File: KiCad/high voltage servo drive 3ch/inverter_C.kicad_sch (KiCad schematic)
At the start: 50 parts, among them U18 IPM

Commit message: prepare rev0.1 for manufacturing
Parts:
- C164, C165, C166, C167, C168, C169, C186: Generic Allowed? (none) -> yes; LCSC# (none) -> C106205; Manufacturer (none) -> YAGEO; Part number (none) -> CC0402KRX7R9BB102; cost (none) -> 0.001
- C170, C172, C175, C185: Generic Allowed? (none) -> yes; LCSC# C7393943 -> C50254; Manufacturer (none) -> Samsung Electro-Mechanics; Part number (none) -> CL31B225KBHNNNE; cost (none) -> 0.03
- C171, C173, C174, C176, C178, C179, C180, C184: Generic Allowed? (none) -> yes; LCSC# (none) -> C105882; Manufacturer (none) -> YAGEO; Part number (none) -> CC0402KRX5R9BB104; cost (none) -> 0.003
- C177, C187: Generic Allowed? (none) -> yes; LCSC# C473196 -> C7471876; Manufacturer (none) -> KNSCHA; Part number (none) -> 189RV0014; cost (none) -> 0.05
- C181, C182: Generic Allowed? (none) -> yes; Manufacturer (none) -> HUI JU; Part number (none) -> NV1812B104K102CEMN; cost (none) -> 0.1447
- C183, C197: Generic Allowed? (none) -> yes; LCSC# (none) -> C60133; Manufacturer (none) -> YAGEO; Part number (none) -> CC0402KRX7R9BB103; cost (none) -> 0.001
- D44, D45, D46, D47: Generic Allowed? (none) -> yes; LCSC# SMA2Z22A -> C7440711; Manufacturer (none) -> XCH; Part number (none) -> SMA2Z22A; cost (none) -> 0.07
- FB10, FB9: value FerriteBead -> 0; Generic Allowed? (none) -> yes; LCSC# C963878 -> C2907406; Manufacturer (none) -> FOJAN; Part number (none) -> FRC1206P000 TS; cost (none) -> 0.0015
- NT7, NT8, NT9: now not fitted
- R114, R115, R116, R117, R118, R119, R121: value 100 -> 120; Generic Allowed? (none) -> yes; LCSC# (none) -> C114758; Manufacturer (none) -> YAGEO; Part number (none) -> RC0402FR-07120RL; cost (none) -> 0.0008
- R120, R140: Generic Allowed? (none) -> yes; LCSC# (none) -> C105873; Manufacturer (none) -> YAGEO; Part number (none) -> RC0402JR-075K1L; cost (none) -> 0.0006
- R122, R123, R124, R125, R126, R127: Generic Allowed? (none) -> yes, 1% or better; LCSC # C7419996 -> (none); LCSC# (none) -> C7419996; Manufacturer (none) -> FOJAN; Part number (none) -> FRM121WFR005TM; cost (none) -> 0.03
- U18: Manufacturer (none) -> ONSEMI; now not fitted

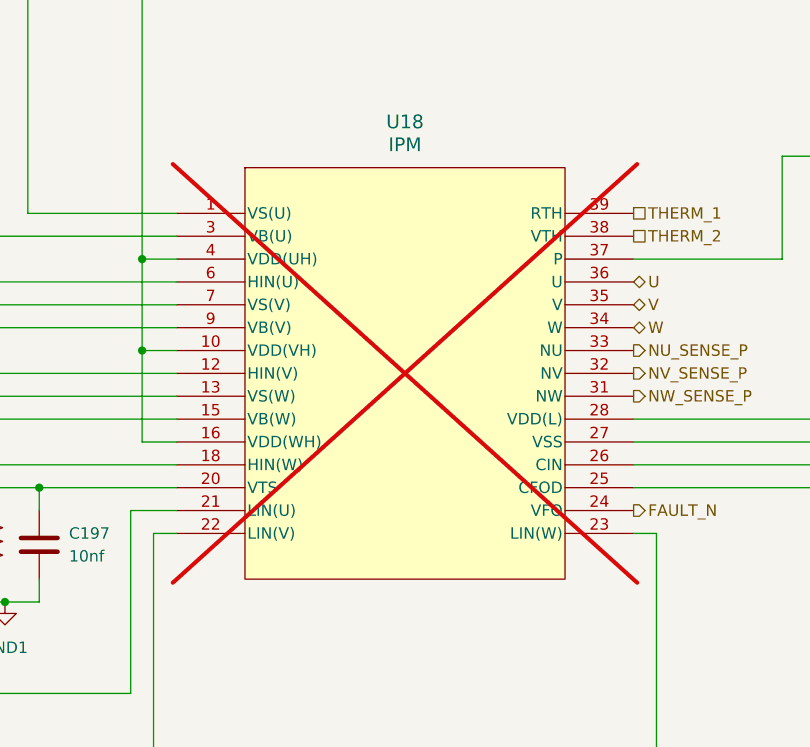
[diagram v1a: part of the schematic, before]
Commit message: update BOM and change transceivers
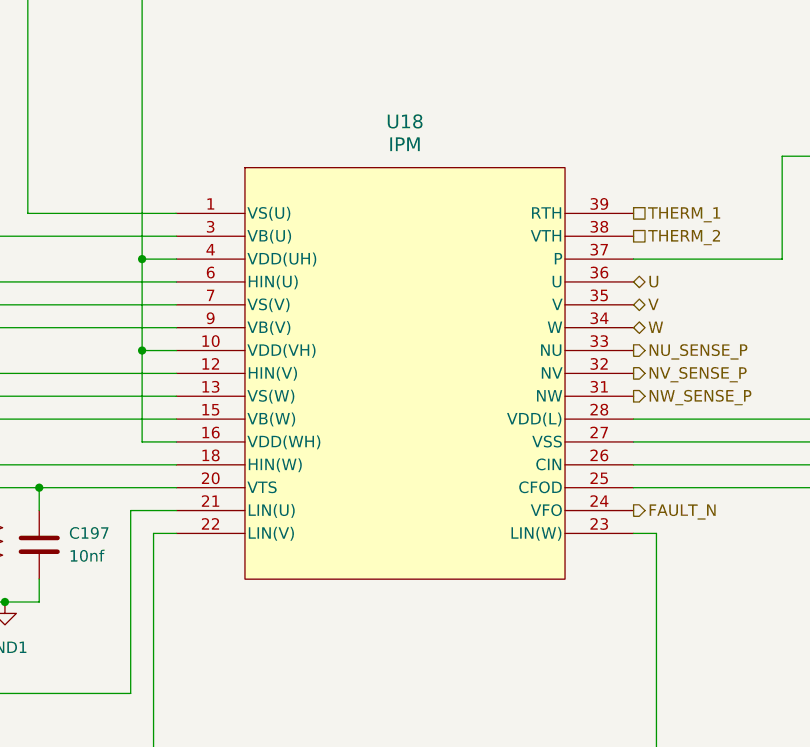
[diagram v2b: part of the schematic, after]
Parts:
- FB10, FB9: LCSC# C2907406 -> C2907288; Part number FRC1206P000 TS -> FRC0805P000 TS
- U18: footprint footprints:DIP39_54.5X31.0_MODGC_OSI -> DIP39_54.5X31.0_MODGC_OSI; now fitted
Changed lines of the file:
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@@
 		(in_bom yes)
 		(on_board yes)
-		(dnp yes)
+		(dnp no)
 		(fields_autoplaced yes)
 		(property "Reference" "U18"
@@
 			)
 		)
-		(property "Footprint" "footprints:DIP39_54.5X31.0_MODGC_OSI"
+		(property "Footprint" "DIP39_54.5X31.0_MODGC_OSI"
 			(at 184.15 121.92 0)
 			(effects
@@
 			)
 		)
-		(property "Datasheet" "IPM"
+		(property "Datasheet" "NFAM3065L4BT"
 			(at 184.15 121.92 0)
 			(effects
@@
 			)
 		)
-		(property "Description" "50v"
+		(property "Description" "Unpolarized capacitor"
 			(at 106.68 157.48 0)
 			(effects
@@
 			)
 		)
-		(property "Description" "50v"
+		(property "Description" "Unpolarized capacitor"
 			(at 116.84 203.2 0)
 			(effects
@@
 			)
 		)
-		(property "Description" "low inductance type"
+		(property "Description" "Resistor, US symbol"
 			(at 344.17 80.01 0)
 			(effects
@@
 			)
 		)
-		(property "Description" "low inductance type"
+		(property "Description" "Resistor, US symbol"
 			(at 344.17 58.42 0)
 			(effects
@@
 			)
 		)
-		(property "Description" "50v"
+		(property "Description" "Unpolarized capacitor"
 			(at 168.91 158.75 0)
 			(effects
@@
 			)
 		)
-		(property "Description" "50v"
+		(property "Description" "Unpolarized capacitor"
 			(at 328.93 158.75 0)
 			(effects
@@
 			)
 		)
-		(property "Description" "50v"
+		(property "Description" "Unpolarized capacitor"
 			(at 184.15 85.09 0)
 			(effects
@@
 			)
 		)
-		(property "Description" "63v"
+		(property "Description" "Polarized capacitor"
 			(at 335.28 143.51 0)
 			(effects
@@
 			)
 		)
-		(property "Description" "50v"
+		(property "Description" "Unpolarized capacitor"
 			(at 106.68 203.2 0)
 			(effects
@@
 			)
 		)
-		(property "Description" "50v"
+		(property "Description" "Unpolarized capacitor"
 			(at 184.15 73.66 0)
 			(effects
@@
 			)
 		)
-		(property "Description" "low inductance type"
+		(property "Description" "Resistor, US symbol"
 			(at 344.17 93.98 0)
 			(effects
@@
 			)
 		)
-		(property "Description" "50v"
+		(property "Description" "Unpolarized capacitor"
 			(at 140.97 85.09 0)
 			(effects
@@
 			)
 		)
-		(property "Description" "50v"
+		(property "Description" "Unpolarized capacitor"
 			(at 184.15 62.23 0)
 			(effects
@@
 			)
 		)
-		(property "Description" "low inductance type"
+		(property "Description" "Resistor, US symbol"
 			(at 344.17 76.2 0)
 			(effects
@@
 			)
 		)
-		(property "Description" "50v"
+		(property "Description" "Unpolarized capacitor"
 			(at 152.4 85.09 0)
 			(effects
@@
 			)
 		)
-		(property "Description" "50v"
+		(property "Description" "Unpolarized capacitor"
 			(at 323.85 143.51 0)
 			(effects
@@
 			)
 		)
-		(property "Description" "50v"
+		(property "Description" "Unpolarized capacitor"
 			(at 316.23 143.51 0)
 			(effects
@@
 			)
 		)
-		(property "LCSC#" "C2907406"
+		(property "LCSC#" "C2907288"
 			(at 316.23 134.62 0)
 			(effects
@@
 			)
 		)
-		(property "Part number" "FRC1206P000 TS"
+		(property "Part number" "FRC0805P000 TS"
 			(at 316.23 134.62 0)
 			(effects
@@
 			)
 		)
-		(property "Description" "50v"
+		(property "Description" "Unpolarized capacitor"
 			(at 163.83 85.09 0)
 			(effects
@@
 			)
 		)
-		(property "Description" "50v"
+		(property "Description" "Unpolarized capacitor"
 			(at 96.52 157.48 0)
 			(effects
@@
 			)
 		)
-		(property "Description" "50v"
+		(property "Description" "Unpolarized capacitor"
 			(at 152.4 73.66 0)
 			(effects
@@
 			)
 		)
-		(property "Description" "low inductance type"
+		(property "Description" "Resistor, US symbol"
 			(at 344.17 97.79 0)
 			(effects
@@
 			)
 		)
-		(property "Description" "50v"
+		(property "Description" "Unpolarized capacitor"
 			(at 163.83 73.66 0)
 			(effects
@@
 			)
 		)
-		(property "LCSC#" "C2907406"
+		(property "LCSC#" "C2907288"
 			(at 176.53 34.29 0)
 			(effects
@@
 			)
 		)
-		(property "Part number" "FRC1206P000 TS"
+		(property "Part number" "FRC0805P000 TS"
 			(at 176.53 34.29 0)
 			(effects
@@
 			)
 		)
-		(property "Description" "50v"
+		(property "Description" "Unpolarized capacitor"
 			(at 96.52 203.2 0)
 			(effects
@@
 			)
 		)
-		(property "Description" "1kv"
+		(property "Description" "Unpolarized capacitor"
 			(at 273.05 120.65 0)
 			(effects
@@
 			)
 		)
-		(property "Description" "50v"
+		(property "Description" "Unpolarized capacitor"
 			(at 307.34 168.91 0)
 			(effects
@@
 			)
 		)
-		(property "Description" "50v"
+		(property "Description" "Unpolarized capacitor"
 			(at 140.97 73.66 0)
 			(effects
@@
 			)
 		)
-		(property "Description" "1kv"
+		(property "Description" "Unpolarized capacitor"
 			(at 285.75 120.65 0)
 			(effects
@@
 			)
 		)
-		(property "Description" "low inductance type"
+		(property "Description" "Resistor, US symbol"
 			(at 344.17 62.23 0)
 			(effects
@@
 			)
 		)
-		(property "Description" "50v"
+		(property "Description" "Unpolarized capacitor"
 			(at 116.84 157.48 0)
 			(effects
@@
 			)
 		)
-		(property "Description" "50v"
+		(property "Description" "Unpolarized capacitor"
 			(at 148.59 156.21 0)
 			(effects
@@
 			)
 		)
-		(property "Description" "63v"
+		(property "Description" "Polarized capacitor"
 			(at 184.15 49.53 0)
 			(effects
